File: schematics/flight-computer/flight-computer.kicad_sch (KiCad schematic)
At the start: 43 parts, among them J101 BATT, J102 GPS, J103 TELEM, J104 Expansion Slot, J105 USB C, J106 SWD, J107 BLACKBOX, U101 STM32F405RGT6, U102 MAX14787E, Y101 26M

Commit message: Add order codes for remaining components
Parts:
- J104: Farnell (none) -> 3226016
- J106: Farnell (none) -> 2856426

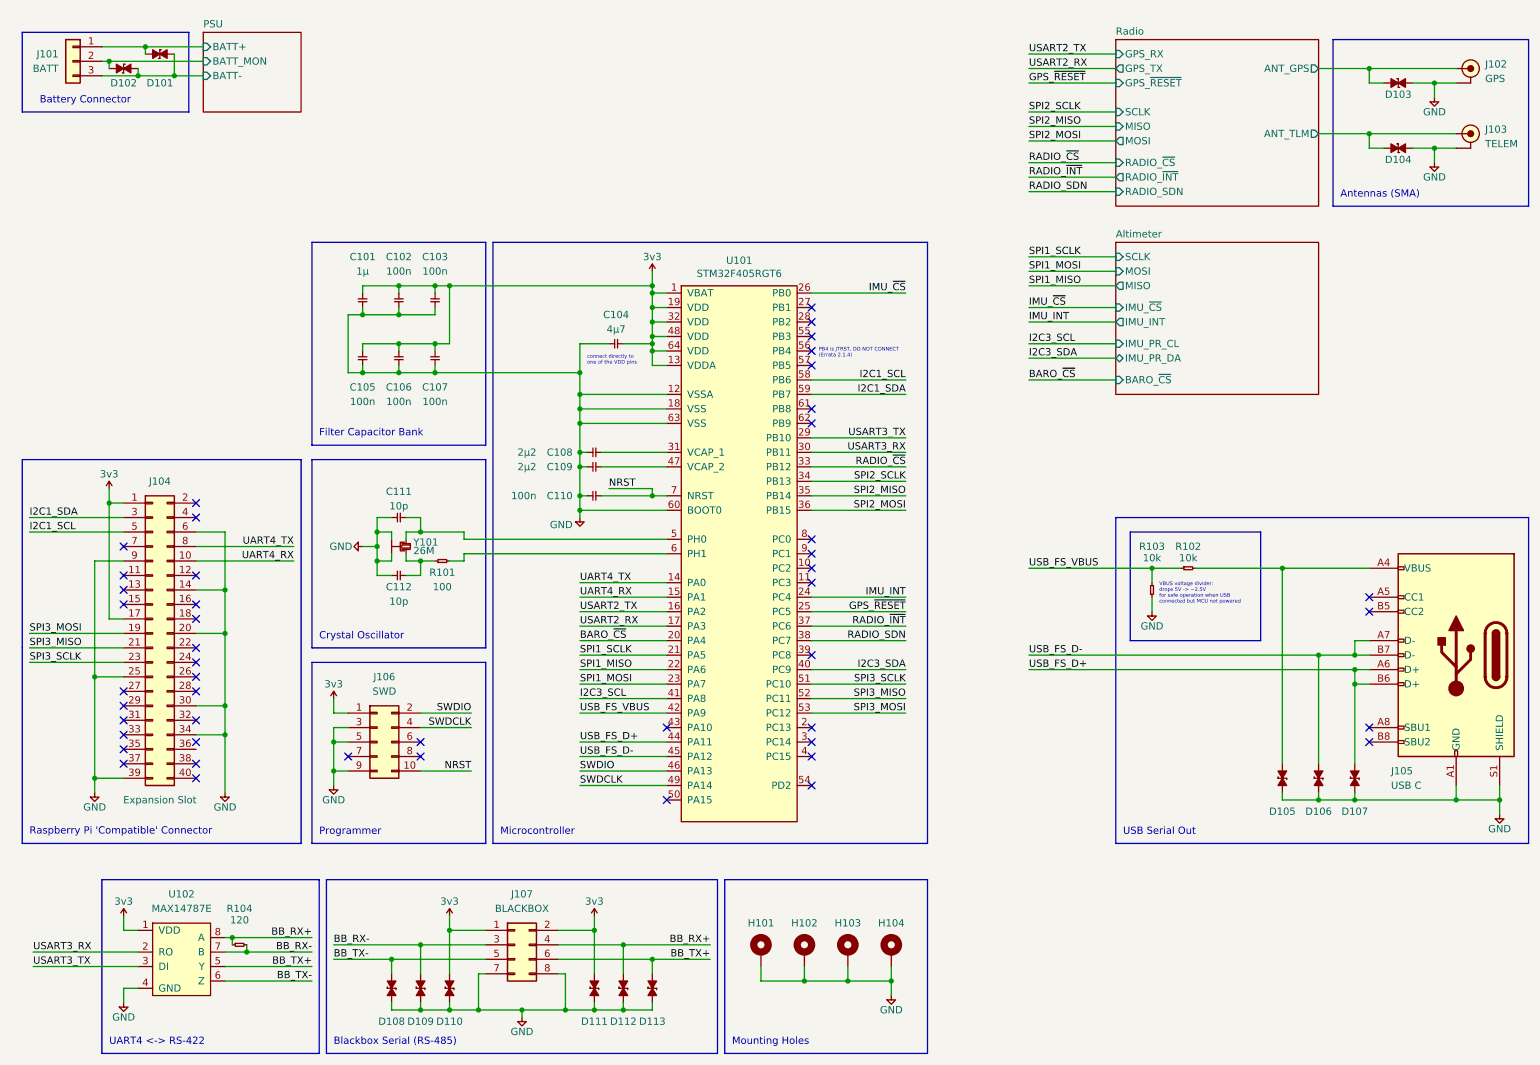
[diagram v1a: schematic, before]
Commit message: Add test points
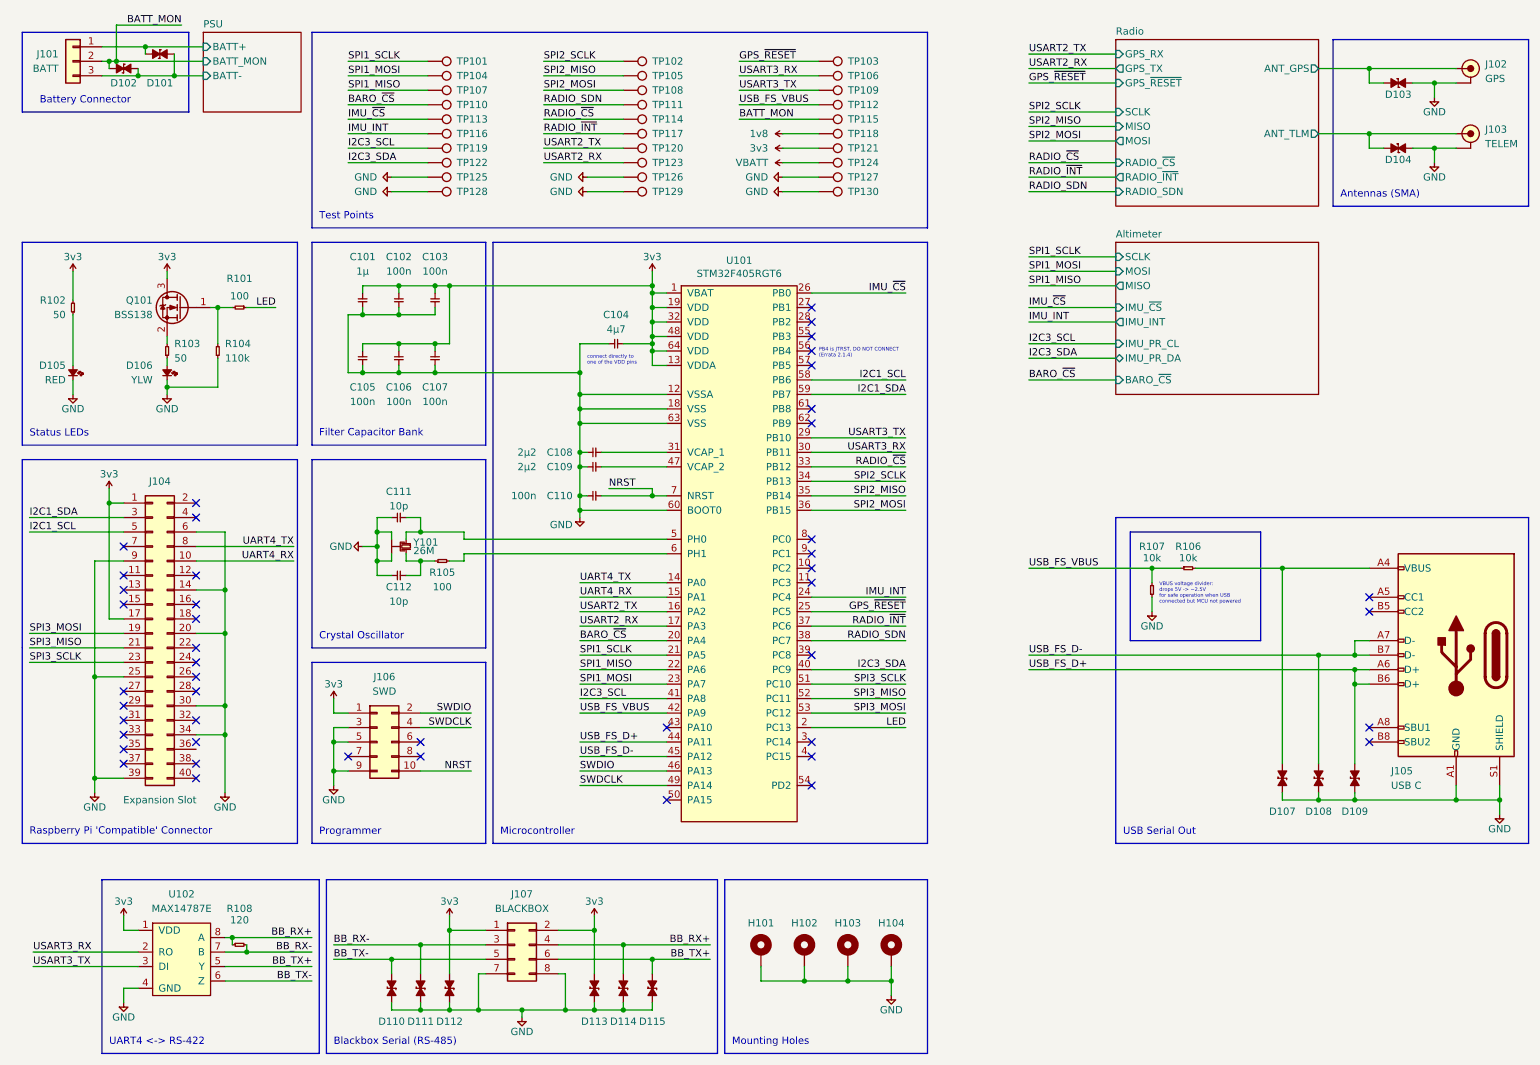
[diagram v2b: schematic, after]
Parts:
- added D105: RED, Strix:LED_0402, symbol Strix:LED
- added D106: YLW, Strix:LED_0402, symbol Strix:LED
- added Q101: BSS138, Strix:BSS138, symbol Strix:BSS138
- added R101: 100, Strix:R_0402, symbol Strix:R
- added R102, R103: 50, Strix:R_0402, symbol Strix:R
- added R104: 110k, Strix:R_0402, symbol Strix:R
- added TP101, TP102, TP103, TP104, TP105, TP106, TP107, TP108, TP109, TP110, TP111, TP112, TP113, TP114, TP115, TP116, TP117, TP118, TP119, TP120, TP121, TP122, TP123, TP124, TP125, TP126, TP127, TP128, TP129, TP130: TestPoint, Strix:TestPoint, symbol Strix:TestPoint
- renumbered D105 to D107, D106 to D108, D107 to D109, D108 to D110, D109 to D111, D110 to D112, D111 to D113, D112 to D114, D113 to D115, R101 to R105, R102 to R106, R103 to R107, R104 to R108
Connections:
- net 3v3: now also Q101.3 (D), R102.2, TP121.1
- net BARO_~{CS}: now also TP110.1
- net GND: now also D105.1, D106.1, R104.1, TP125.1, TP126.1, TP127.1, TP128.1, TP129.1, TP130.1
- net GPS_~{RESET}: now also TP103.1
- net I2C3_SCL: now also TP119.1
- net I2C3_SDA: now also TP122.1
- net IMU_INT: now also TP116.1
- net IMU_~{CS}: now also TP113.1
- net RADIO_SDN: now also TP111.1
- net RADIO_~{CS}: now also TP114.1
- net RADIO_~{INT}: now also TP117.1
- net SPI1_MISO: now also TP107.1
- net SPI1_MOSI: now also TP104.1
- net SPI1_SCLK: now also TP101.1
- net SPI2_MISO: now also TP105.1
- net SPI2_MOSI: now also TP108.1
- net SPI2_SCLK: now also TP102.1
- net USART2_RX: now also TP123.1
- net USART2_TX: now also TP120.1
- net USART3_RX: now also TP106.1
- net USART3_TX: now also TP109.1
- net USB_FS_VBUS: now also TP112.1
- net LED: now reaches U101.2 (PC13)
- net LED: now also R101.1
- net PSU/BATT_MON renamed BATT_MON
- net BATT_MON: now also TP115.1
- new net: D105.2, R102.1
- new net: D106.2, R103.1
- new net: Q101.1 (G), R101.2, R104.2
- new net: Q101.2 (S), R103.2
- new net 1v8: TP118.1
- new net VBATT: TP124.1
- no-connect marks 48 -> 47
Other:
- note added: "Status LEDs"
- note added: "Test Points"

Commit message: Final changes for manufacture
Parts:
- C101: Farnell 2496814 -> 1759436
- C104: Farnell 2426952 -> 2211173
- Q101: Farnell (none) -> 2053833
- R101: Farnell (none) -> 2331443
- R102, R103: Farnell (none) -> 3544456
- R104: Farnell (none) -> 2059181
